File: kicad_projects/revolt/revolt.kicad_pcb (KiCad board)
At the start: 2 copper layers, 143.5 x 111.4 mm, 68 parts

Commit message: todos, remove fp info cache
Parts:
- added J1: IDC-Header_2x07_P2.54mm_Vertical, Connector_IDC:IDC-Header_2x07_P2.54mm_Vertical, F.Cu at (215.1, 66.8)
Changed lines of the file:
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@@
   (net 45 "/COL5")
   (net 46 "/COL6")
+  (net 47 "unconnected-(J1-Pin_1-Pad1)")
+  (net 48 "unconnected-(J1-Pin_2-Pad2)")
+  (net 49 "unconnected-(J1-Pin_3-Pad3)")
+  (net 50 "unconnected-(J1-Pin_4-Pad4)")
+  (net 51 "unconnected-(J1-Pin_5-Pad5)")
+  (net 52 "unconnected-(J1-Pin_6-Pad6)")
+  (net 53 "unconnected-(J1-Pin_7-Pad7)")
+  (net 54 "unconnected-(J1-Pin_8-Pad8)")
+  (net 55 "unconnected-(J1-Pin_9-Pad9)")
+  (net 56 "unconnected-(J1-Pin_10-Pad10)")
+  (net 57 "unconnected-(J1-Pin_11-Pad11)")
+  (net 58 "unconnected-(J1-Pin_12-Pad12)")
+  (net 59 "unconnected-(J1-Pin_13-Pad13)")
+  (net 60 "unconnected-(J1-Pin_14-Pad14)")
   (footprint "ComboDiode" (layer "F.Cu")
     (at 212.852 106.045 180)
@@
       (net 5 "Net-(D5-A)") (pinfunction "2") (pintype "passive"))
   )
+  (footprint "Connector_IDC:IDC-Header_2x07_P2.54mm_Vertical" (layer "F.Cu")
+    (at 215.138 66.802)
+    (descr "Through hole IDC box header, 2x07, 2.54mm pitch, DIN 41651 / IEC 60603-13, double rows, https://docs.google.com/spreadsheets/d/16SsEcesNF15N3Lb4niX7dcUr-NY5_MFPQhobNuNppn4/edit#gid=0")
+    (tags "Through hole vertical IDC box header THT 2x07 2.54mm double row")
+    (property "Sheetfile" "revolt.kicad_sch")
+    (property "Sheetname" "")
+    (property "ki_description" "Generic connector, double row, 02x07, counter clockwise pin numbering scheme (similar to DIP package numbering), script generated (kicad-library-utils/schlib/autogen/connector/)")
+    (property "ki_keywords" "connector")
+    (attr through_hole)
+    (fp_text reference "J1" (at 1.27 -6.1) (layer "F.SilkS")
+        (effects (font (size 1 1) (thickness 0.15)))
+    )
+    (fp_text value "IDC-Header_2x07_P2.54mm_Vertical" (at 1.27 21.34) (layer "F.Fab")
+        (effects (font (size 1 1) (thickness 0.15)))
+    )
+    (fp_text user "${REFERENCE}" (at 1.27 7.62 90) (layer "F.Fab")
+        (effects (font (size 1 1) (thickness 0.15)))
+    )
+    (fp_line (start -4.68 -0.5) (end -4.68 0.5)
+      (stroke (width 0.12) (type solid)) (layer "F.SilkS"))
+    (fp_line (start -4.68 0.5) (end -3.68 0)
+      (stroke (width 0.12) (type solid)) (layer "F.SilkS"))
+    (fp_line (start -3.68 0) (end -4.68 -0.5)
+      (stroke (width 0.12) (type solid)) (layer "F.SilkS"))
+    (fp_line (start -3.29 -5.21) (end 5.83 -5.21)
+      (stroke (width 0.12) (type solid)) (layer "F.SilkS"))
+    (fp_line (start -3.29 5.57) (end -1.98 5.57)
+      (stroke (width 0.12) (type solid)) (layer "F.SilkS"))
+    (fp_line (start -3.29 20.45) (end -3.29 -5.21)
+      (stroke (width 0.12) (type solid)) (layer "F.SilkS"))
+    (fp_line (start -1.98 -3.91) (end 4.52 -3.91)
+      (stroke (width 0.12) (type solid)) (layer "F.SilkS"))
+    (fp_line (start -1.98 5.57) (end -1.98 -3.91)
+      (stroke (width 0.12) (type solid)) (layer "F.SilkS"))
+    (fp_line (start -1.98 9.67) (end -3.29 9.67)
+      (stroke (width 0.12) (type solid)) (layer "F.SilkS"))
+    (fp_line (start -1.98 9.67) (end -1.98 9.67)
+      (stroke (width 0.12) (type solid)) (layer "F.SilkS"))
+    (fp_line (start -1.98 19.15) (end -1.98 9.67)
+      (stroke (width 0.12) (type solid)) (layer "F.SilkS"))
+    (fp_line (start 4.52 -3.91) (end 4.52 19.15)
+      (stroke (width 0.12) (type solid)) (layer "F.SilkS"))
+    (fp_line (start 4.52 19.15) (end -1.98 19.15)
+      (stroke (width 0.12) (type solid)) (layer "F.SilkS"))
+    (fp_line (start 5.83 -5.21) (end 5.83 20.45)
+      (stroke (width 0.12) (type solid)) (layer "F.SilkS"))
+    (fp_line (start 5.83 20.45) (end -3.29 20.45)
+      (stroke (width 0.12) (type solid)) (layer "F.SilkS"))
+    (fp_line (start -3.68 -5.6) (end -3.68 20.84)
+      (stroke (width 0.05) (type solid)) (layer "F.CrtYd"))
+    (fp_line (start -3.68 20.84) (end 6.22 20.84)
+      (stroke (width 0.05) (type solid)) (layer "F.CrtYd"))
+    (fp_line (start 6.22 -5.6) (end -3.68 -5.6)
+      (stroke (width 0.05) (type solid)) (layer "F.CrtYd"))
+    (fp_line (start 6.22 20.84) (end 6.22 -5.6)
+      (stroke (width 0.05) (type solid)) (layer "F.CrtYd"))
+    (fp_line (start -3.18 -4.1) (end -2.18 -5.1)
+      (stroke (width 0.1) (type solid)) (layer "F.Fab"))
+    (fp_line (start -3.18 5.57) (end -1.98 5.57)
+      (stroke (width 0.1) (type solid)) (layer "F.Fab"))
+    (fp_line (start -3.18 20.34) (end -3.18 -4.1)
+      (stroke (width 0.1) (type solid)) (layer "F.Fab"))
+    (fp_line (start -2.18 -5.1) (end 5.72 -5.1)
+      (stroke (width 0.1) (type solid)) (layer "F.Fab"))
+    (fp_line (start -1.98 -3.91) (end 4.52 -3.91)
+      (stroke (width 0.1) (type solid)) (layer "F.Fab"))
+    (fp_line (start -1.98 5.57) (end -1.98 -3.91)
+      (stroke (width 0.1) (type solid)) (layer "F.Fab"))
+    (fp_line (start -1.98 9.67) (end -3.18 9.67)
+      (stroke (width 0.1) (type solid)) (layer "F.Fab"))
+    (fp_line (start -1.98 9.67) (end -1.98 9.67)
+      (stroke (width 0.1) (type solid)) (layer "F.Fab"))
+    (fp_line (start -1.98 19.15) (end -1.98 9.67)
+      (stroke (width 0.1) (type solid)) (layer "F.Fab"))
+    (fp_line (start 4.52 -3.91) (end 4.52 19.15)
+      (stroke (width 0.1) (type solid)) (layer "F.Fab"))
+    (fp_line (start 4.52 19.15) (end -1.98 19.15)
+      (stroke (width 0.1) (type solid)) (layer "F.Fab"))
+    (fp_line (start 5.72 -5.1) (end 5.72 20.34)
+      (stroke (width 0.1) (type solid)) (layer "F.Fab"))
+    (fp_line (start 5.72 20.34) (end -3.18 20.34)
+      (stroke (width 0.1) (type solid)) (layer "F.Fab"))
+    (pad "1" thru_hole roundrect (at 0 0) (size 1.7 1.7) (drill 1) (layers "*.Cu" "*.Mask") (roundrect_rratio 0.147059)
+      (net 47 "unconnected-(J1-Pin_1-Pad1)") (pinfunction "Pin_1") (pintype "passive"))
+    (pad "2" thru_hole circle (at 2.54 0) (size 1.7 1.7) (drill 1) (layers "*.Cu" "*.Mask")
+      (net 48 "unconnected-(J1-Pin_2-Pad2)") (pinfunction "Pin_2") (pintype "passive"))
+    (pad "3" thru_hole circle (at 0 2.54) (size 1.7 1.7) (drill 1) (layers "*.Cu" "*.Mask")
+      (net 49 "unconnected-(J1-Pin_3-Pad3)") (pinfunction "Pin_3") (pintype "passive"))
+    (pad "4" thru_hole circle (at 2.54 2.54) (size 1.7 1.7) (drill 1) (layers "*.Cu" "*.Mask")
+      (net 50 "unconnected-(J1-Pin_4-Pad4)") (pinfunction "Pin_4") (pintype "passive"))
+    (pad "5" thru_hole circle (at 0 5.08) (size 1.7 1.7) (drill 1) (layers "*.Cu" "*.Mask")
+      (net 51 "unconnected-(J1-Pin_5-Pad5)") (pinfunction "Pin_5") (pintype "passive"))
+    (pad "6" thru_hole circle (at 2.54 5.08) (size 1.7 1.7) (drill 1) (layers "*.Cu" "*.Mask")
+      (net 52 "unconnected-(J1-Pin_6-Pad6)") (pinfunction "Pin_6") (pintype "passive"))
+    (pad "7" thru_hole circle (at 0 7.62) (size 1.7 1.7) (drill 1) (layers "*.Cu" "*.Mask")
+      (net 53 "unconnected-(J1-Pin_7-Pad7)") (pinfunction "Pin_7") (pintype "passive"))
+    (pad "8" thru_hole circle (at 2.54 7.62) (size 1.7 1.7) (drill 1) (layers "*.Cu" "*.Mask")
+      (net 54 "unconnected-(J1-Pin_8-Pad8)") (pinfunction "Pin_8") (pintype "passive"))
+    (pad "9" thru_hole circle (at 0 10.16) (size 1.7 1.7) (drill 1) (layers "*.Cu" "*.Mask")
+      (net 55 "unconnected-(J1-Pin_9-Pad9)") (pinfunction "Pin_9") (pintype "passive"))
+    (pad "10" thru_hole circle (at 2.54 10.16) (size 1.7 1.7) (drill 1) (layers "*.Cu" "*.Mask")
+      (net 56 "unconnected-(J1-Pin_10-Pad10)") (pinfunction "Pin_10") (pintype "passive"))
+    (pad "11" thru_hole circle (at 0 12.7) (size 1.7 1.7) (drill 1) (layers "*.Cu" "*.Mask")
+      (net 57 "unconnected-(J1-Pin_11-Pad11)") (pinfunction "Pin_11") (pintype "passive"))
+    (pad "12" thru_hole circle (at 2.54 12.7) (size 1.7 1.7) (drill 1) (layers "*.Cu" "*.Mask")
+      (net 58 "unconnected-(J1-Pin_12-Pad12)") (pinfunction "Pin_12") (pintype "passive"))
+    (pad "13" thru_hole circle (at 0 15.24) (size 1.7 1.7) (drill 1) (layers "*.Cu" "*.Mask")
+      (net 59 "unconnected-(J1-Pin_13-Pad13)") (pinfunction "Pin_13") (pintype "passive"))
+    (pad "14" thru_hole circle (at 2.54 15.24) (size 1.7 1.7) (drill 1) (layers "*.Cu" "*.Mask")
+      (net 60 "unconnected-(J1-Pin_14-Pad14)") (pinfunction "Pin_14") (pintype "passive"))
+    (model "${KICAD6_3DMODEL_DIR}/Connector_IDC.3dshapes/IDC-Header_2x07_P2.54mm_Vertical.wrl"
+      (offset (xyz 0 0 0))
+      (scale (xyz 1 1 1))
+      (rotate (xyz 0 0 0))
+    )
+  )
   (footprint "keyswitches:SW_PG1350_reversible" (layer "F.Cu")
     (at 120.142 134.874)
@@
       (net 22 "Net-(D22-A)") (pinfunction "A") (pintype "passive"))
   )
+  (gr_circle (center 207.264 66.802) (end 210.264 66.802)
+    (stroke (width 0.2) (type default)) (fill none) (layer "F.Cu"))
   (gr_line (start 124.715324 60.833) (end 220.123 60.833)
     (stroke (width 0.15) (type solid)) (layer "Edge.Cuts"))

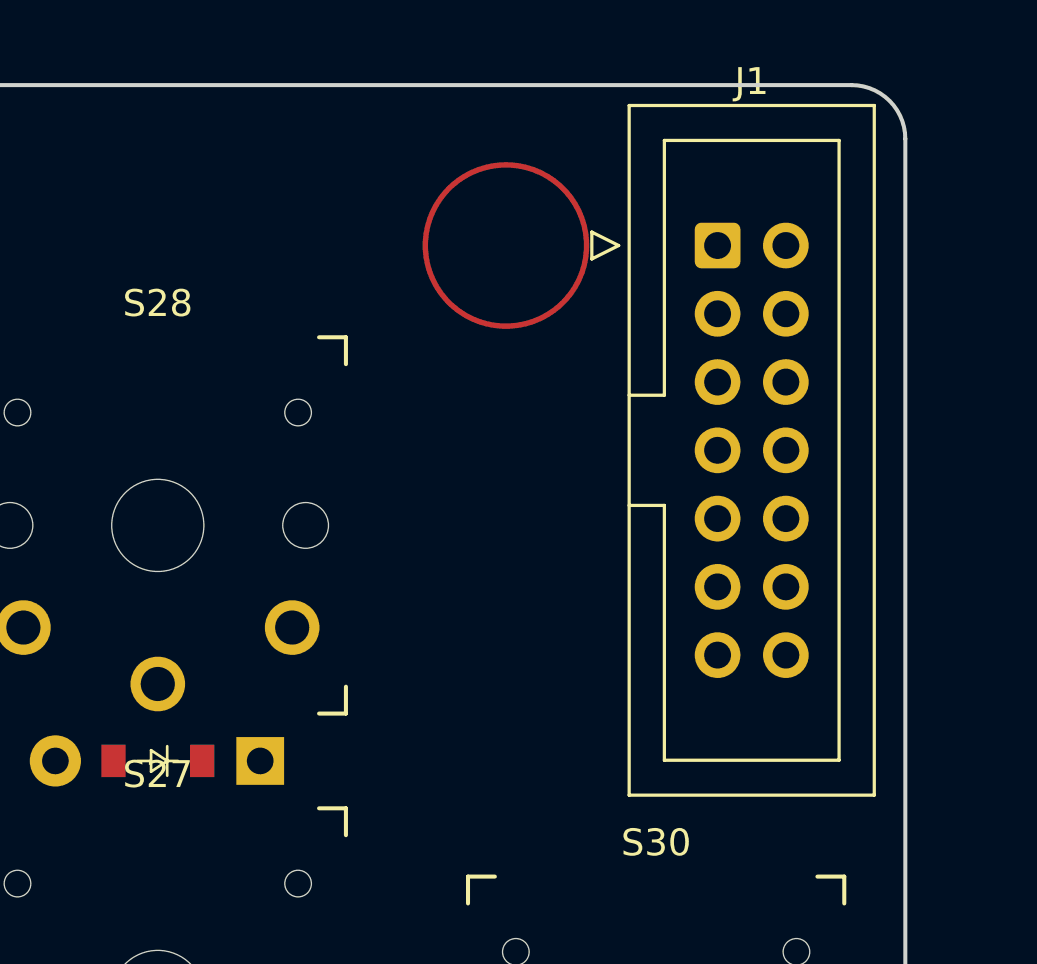
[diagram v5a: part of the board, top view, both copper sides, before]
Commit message: Add library with custom footprints
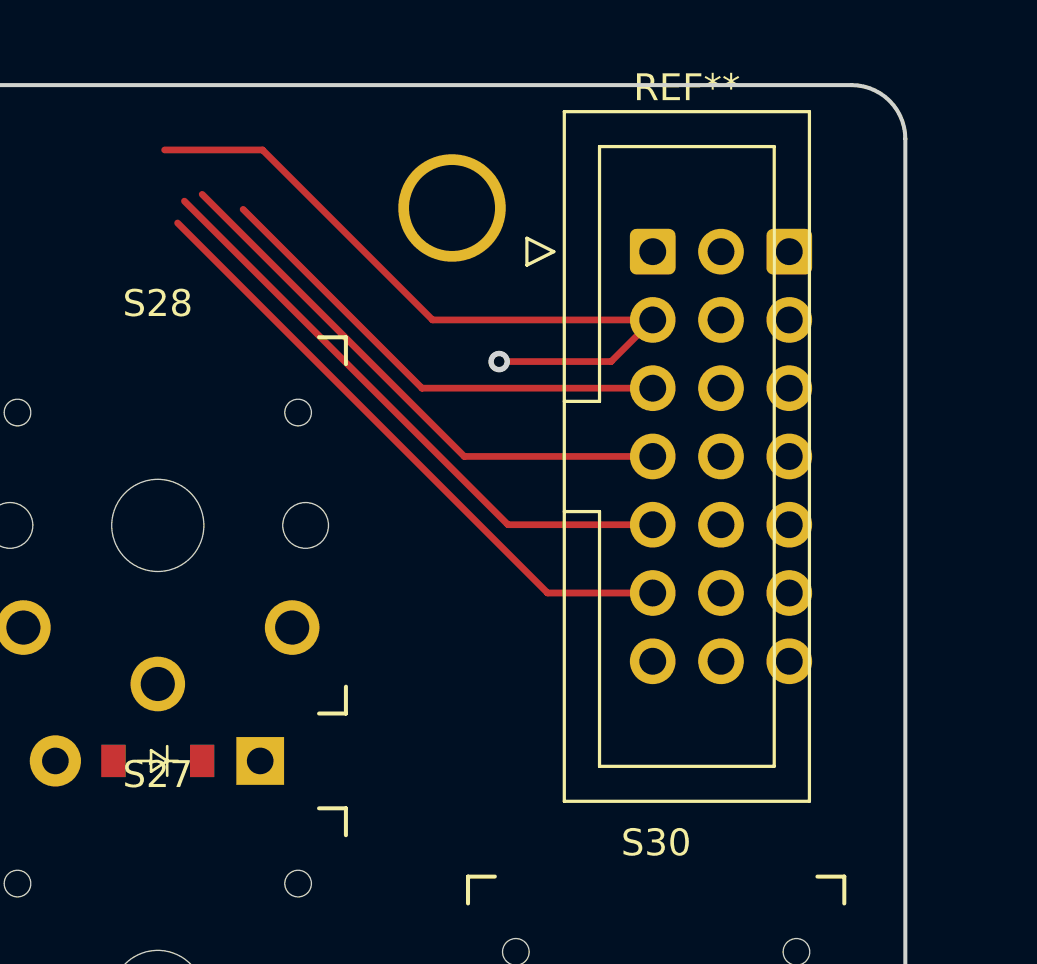
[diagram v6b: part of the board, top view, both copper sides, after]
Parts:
- removed J1: IDC-Header_2x07_P2.54mm_Vertical, Connector_IDC:IDC-Header_2x07_P2.54mm_Vertical
- added HOLE_M3: VAL**, revolt_footprints:HOLE_M3, F.Cu at (205.3, 65.4)
- added REF**: IDC-Header_2x07_P2.54mm_Vertical_Reversible, revolt_footprints:IDC-Header_2x07_P2.54mm_Vertical_Reversible, F.Cu at (212.7, 67.0)
- S1, S10, S11, S12, S13, S14, S15, S16, S17, S18, S19, S2, S20, S21, S22, S23, S24, S25, S26, S27, S28, S29, S3, S30, S31, S32, S33, S34, S4, S5, S6, S7, S8, S9: footprint keyswitches:SW_PG1350_reversible -> revolt_footprints:SW_PG1350_reversible_with_keycap_outline
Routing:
- net (no net): track 0.00 -> 113.1 mm, vias 0 -> 1

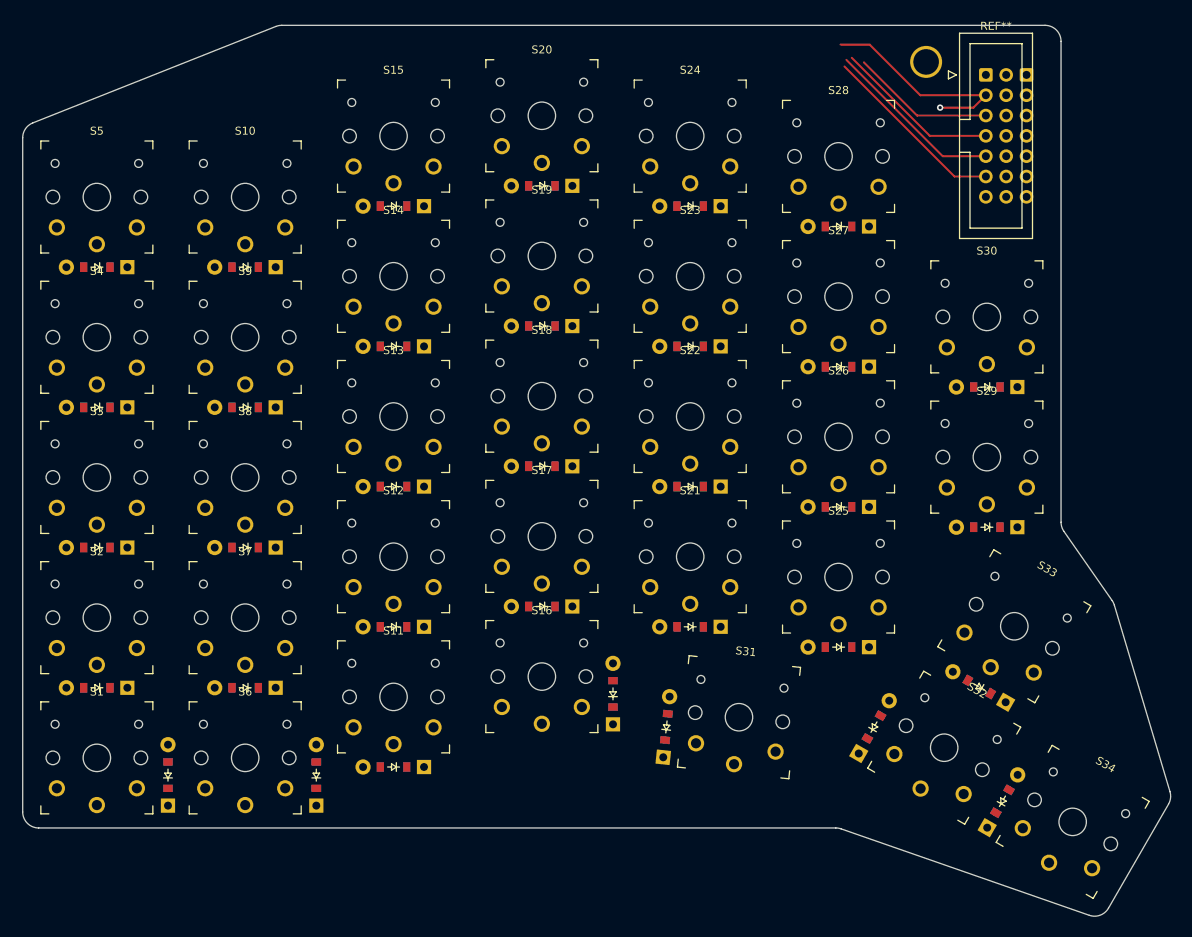
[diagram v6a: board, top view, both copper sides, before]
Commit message: Make the outline universal for hotswap and regular switches
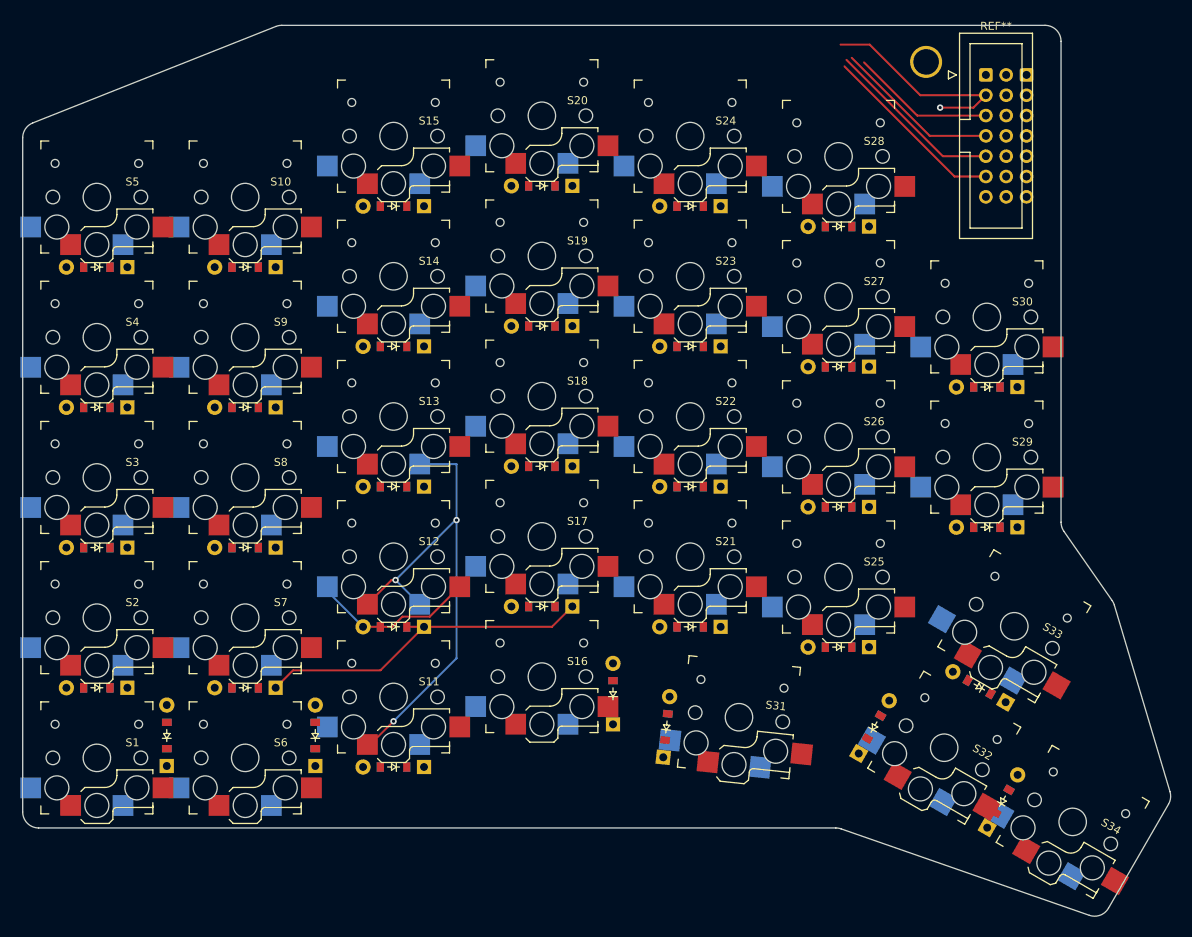
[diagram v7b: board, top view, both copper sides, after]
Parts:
- S1, S10, S11, S12, S13, S14, S15, S16, S17, S18, S19, S2, S20, S21, S22, S23, S24, S25, S26, S27, S28, S29, S3, S30, S31, S32, S33, S34, S4, S5, S6, S7, S8, S9: footprint revolt_footprints:SW_PG1350_reversible_with_keycap_outline -> keyswitches:Kailh_socket_PG1350_reversible
- moved D1 4.96 mm to (110.3, 149.6)
- moved D6 4.95 mm to (128.9, 149.6)
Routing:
- net /COL2: track 0.00 -> 64.3 mm, vias 0 -> 3
- net /ROW3: track 0.00 -> 43.5 mm
- net Net-(D12-A): track 0.00 -> 21.0 mm

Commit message: Base design, need to unify and double-check DRD rules
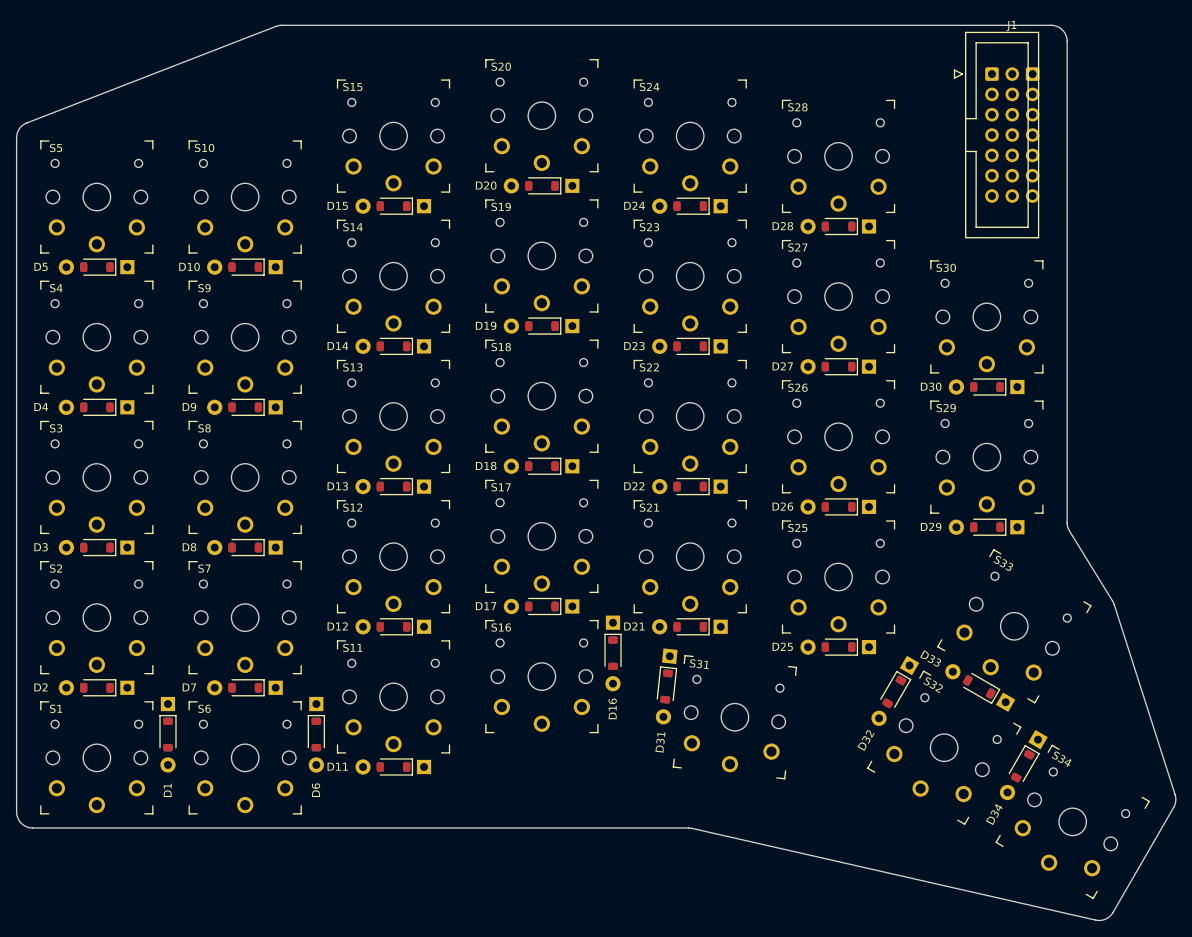
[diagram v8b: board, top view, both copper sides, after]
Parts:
- removed HOLE_M3: VAL**, revolt_footprints:HOLE_M3
- removed REF**: IDC-Header_2x07_P2.54mm_Vertical_Reversible, revolt_footprints:IDC-Header_2x07_P2.54mm_Vertical_Reversible
- added J1: IDC-Header_2x07_P2.54mm_Vertical_Reversible, revolt_footprints:IDC-Header_2x07_P2.54mm_Vertical_Reversible, F.Cu at (213.5, 66.9)
- D1, D10, D11, D12, D13, D14, D15, D16, D17, D18, D19, D2, D20, D21, D22, D23, D24, D25, D26, D27, D28, D29, D3, D30, D31, D32, D33, D34, D4, D5, D6, D7, D8, D9: footprint ComboDiode -> revolt_footprints:D_SOD-123-combo-reversible
- S1, S10, S11, S12, S13, S14, S15, S16, S17, S18, S19, S2, S20, S21, S22, S23, S24, S25, S26, S27, S28, S29, S3, S30, S31, S32, S33, S34, S4, S5, S6, S7, S8, S9: footprint keyswitches:Kailh_socket_PG1350_reversible -> revolt_footprints:SW_PG1350_reversible_with_keycap_outline
- moved D16 5.08 mm to (166.1, 139.3), turned to -90 degrees
- moved D32 5.08 mm to (201.3, 144.2), turned to -120 degrees
- moved D34 5.08 mm to (217.3, 153.4), turned to -120 degrees
- moved D31 5.05 mm to (172.8, 143.5), turned to -96 degrees
- moved S31 0.51 mm to (181.4, 147.3)
- moved D1 0.20 mm to (110.5, 149.5), turned to -90 degrees
- moved D6 0.18 mm to (129.0, 149.5), turned to -90 degrees
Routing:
- net (no net): track 113.1 -> 0.00 mm, vias 1 -> 0
- net /COL2: track 64.3 -> 0.00 mm, vias 3 -> 0
- net /ROW3: track 43.5 -> 0.00 mm
- net Net-(D12-A): track 21.0 -> 0.00 mm
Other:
- board size 143.5 x 111.4 mm -> 144.9 x 111.9 mm
